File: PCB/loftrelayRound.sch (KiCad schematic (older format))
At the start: 27 parts, among them J1 PowerIn, J2 Load, J3 SenSor, J4 Program, K1 G5Q-14-EU DC5, Q1 2N7002, U1 AP1117-33, U2 PC817, U4 ESP-12E

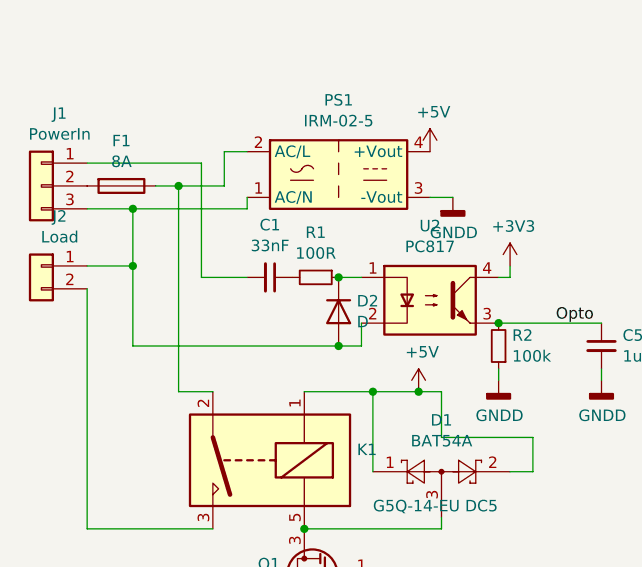
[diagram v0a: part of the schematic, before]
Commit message: Ændret stik
Har ændret til til 3mm mikrofit fjernet C ved optocobler for at undgå stød.
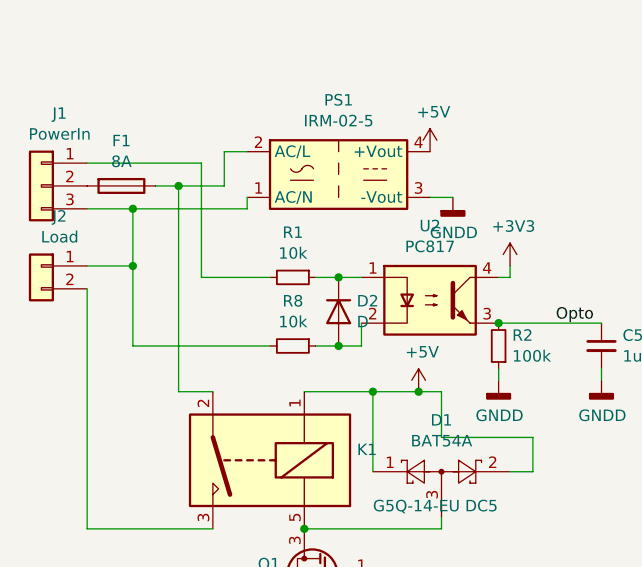
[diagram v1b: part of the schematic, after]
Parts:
- removed C1: 33nF, Capacitors_THT:C_Axial_L5.1mm_D3.1mm_P7.50mm_Horizontal, symbol Device:C_Small
- added R8: 10k, Resistor_SMD:R_1206_3216Metric, symbol Device:R_Small
- J1: footprint Connectors_Molex:Molex_NanoFit_1x03x2.50mm_Straight -> Connector_Molex:Molex_Micro-Fit_3.0_43650-0315_1x03_P3.00mm_Vertical
- J2: footprint Connectors_Molex:Molex_NanoFit_1x02x2.50mm_Straight -> Connector_Molex:Molex_Micro-Fit_3.0_43650-0215_1x02_P3.00mm_Vertical
- R1: value 100R -> 10k; footprint Resistors_SMD:R_1206_HandSoldering -> Resistor_SMD:R_1206_3216Metric
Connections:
- wire segments 85 -> 87
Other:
- moved on the sheet: R1
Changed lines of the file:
@@
-$EndComp
-$Comp
-L Device:C_Small C1
-U 1 1 5BA2C4FB
-P 3350 3050
-F 0 "C1" V 3121 3050 50  0000 C CNN
-F 1 "33nF" V 3212 3050 50  0000 C CNN
-F 2 "Capacitors_THT:C_Axial_L5.1mm_D3.1mm_P7.50mm_Horizontal" H 3350 3050 50  0001 C CNN
-F 3 "~" H 3350 3050 50  0001 C CNN
-	1    3350 3050
-	0    1    1    0
 $EndComp
 $Comp
 L Device:R_Small R1
 U 1 1 5BA2C593
-P 3550 3050
-F 0 "R1" V 3354 3050 50  0000 C CNN
-F 1 "100R" V 3445 3050 50  0000 C CNN
-F 2 "Resistors_SMD:R_1206_HandSoldering" H 3550 3050 50  0001 C CNN
-F 3 "~" H 3550 3050 50  0001 C CNN
-	1    3550 3050
+P 3450 3050
+F 0 "R1" V 3254 3050 50  0000 C CNN
+F 1 "10k" V 3345 3050 50  0000 C CNN
+F 2 "Resistor_SMD:R_1206_3216Metric" H 3450 3050 50  0001 C CNN
+F 3 "~" H 3450 3050 50  0001 C CNN
+	1    3450 3050
 	0    1    1    0
 $EndComp
@@
 F 0 "J1" H 2270 2967 50  0000 C CNN
 F 1 "PowerIn" H 2270 2876 50  0000 C CNN
-F 2 "Connectors_Molex:Molex_NanoFit_1x03x2.50mm_Straight" H 2350 2650 50  0001 C CNN
+F 2 "Connector_Molex:Molex_Micro-Fit_3.0_43650-0315_1x03_P3.00mm_Vertical" H 2350 2650 50  0001 C CNN
 F 3 "~" H 2350 2650 50  0001 C CNN
 	1    2350 2650
@@
 F 0 "J2" H 2270 3217 50  0000 C CNN
 F 1 "Load" H 2270 3126 50  0000 C CNN
-F 2 "Connectors_Molex:Molex_NanoFit_1x02x2.50mm_Straight" H 2350 3000 50  0001 C CNN
+F 2 "Connector_Molex:Molex_Micro-Fit_3.0_43650-0215_1x02_P3.00mm_Vertical" H 2350 3000 50  0001 C CNN
 F 3 "~" H 2350 3000 50  0001 C CNN
 	1    2350 3000
@@
 Wire Wire Line
 	3050 2550 3050 3050
-Wire Wire Line
-	3050 3050 3250 3050
 Connection ~ 2750 2750
 Wire Wire Line
@@
 Wire Wire Line
 	2750 2750 2750 3000
-Wire Wire Line
-	2750 3350 3650 3350
 Connection ~ 3650 3050
-Connection ~ 3650 3350
 Wire Wire Line
 	3650 3350 3750 3350
@@
 Wire Wire Line
 	4350 3250 4800 3250
+$Comp
+L Device:R_Small R8
+U 1 1 5F223F8A
+P 3450 3350
+F 0 "R8" V 3254 3350 50  0000 C CNN
+F 1 "10k" V 3345 3350 50  0000 C CNN
+F 2 "Resistor_SMD:R_1206_3216Metric" H 3450 3350 50  0001 C CNN
+F 3 "~" H 3450 3350 50  0001 C CNN
+	1    3450 3350
+	0    1    1    0
+$EndComp
+Wire Wire Line
+	3650 3050 3550 3050
+Wire Wire Line
+	3050 3050 3350 3050
+Wire Wire Line
+	3650 3350 3550 3350
+Connection ~ 3650 3350
+Wire Wire Line
+	3350 3350 2750 3350
 $EndSCHEMATC

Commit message: Update af komponeter samt ny programmer
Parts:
- Q1: value 2N7002 -> Sq2318AES
- R1: value 10k -> 33K
- R8: value 10k -> 33k
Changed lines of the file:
@@
 P 3450 3050
 F 0 "R1" V 3254 3050 50  0000 C CNN
-F 1 "10k" V 3345 3050 50  0000 C CNN
+F 1 "33K" V 3345 3050 50  0000 C CNN
 F 2 "Resistor_SMD:R_1206_3216Metric" H 3450 3050 50  0001 C CNN
 F 3 "~" H 3450 3050 50  0001 C CNN
@@
 P 3600 4350
 F 0 "Q1" H 3806 4396 50  0000 L CNN
-F 1 "2N7002" H 3806 4305 50  0000 L CNN
+F 1 "Sq2318AES" H 3806 4305 50  0000 L CNN
 F 2 "TO_SOT_Packages_SMD:SOT-23" H 3800 4275 50  0001 L CIN
 F 3 "https://www.fairchildsemi.com/datasheets/2N/2N7002.pdf" H 3600 4350 50  0001 L CNN
@@
 P 3450 3350
 F 0 "R8" V 3254 3350 50  0000 C CNN
-F 1 "10k" V 3345 3350 50  0000 C CNN
+F 1 "33k" V 3345 3350 50  0000 C CNN
 F 2 "Resistor_SMD:R_1206_3216Metric" H 3450 3350 50  0001 C CNN
 F 3 "~" H 3450 3350 50  0001 C CNN

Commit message: 3d footprint
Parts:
- K1: footprint Relays_THT:Relay_SPST_OMRON-G5Q -> Relay_THT:Relay_SPST_Omron-G5Q-1A
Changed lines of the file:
@@
 F 0 "K1" H 2870 3804 50  0000 R CNN
 F 1 "G5Q-14-EU DC5" H 2800 4050 50  0000 R CNN
-F 2 "Relays_THT:Relay_SPST_OMRON-G5Q" H 3650 3800 50  0001 L CNN
+F 2 "Relay_THT:Relay_SPST_Omron-G5Q-1A" H 3650 3800 50  0001 L CNN
 F 3 "https://www.omron.com/ecb/products/pdf/en-g5q.pdf" H 4400 3550 50  0001 C CNN
 	1    3300 3850

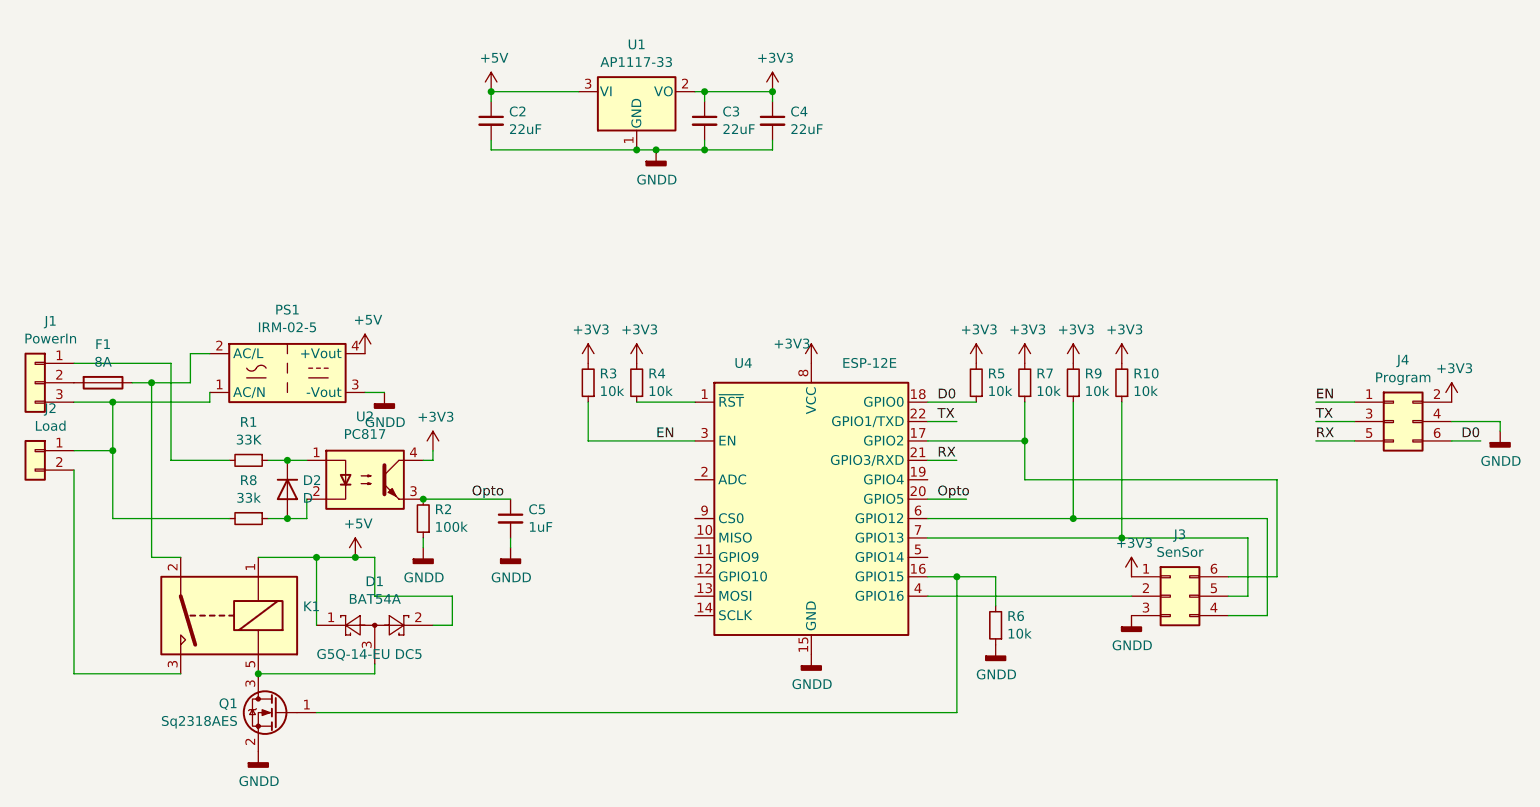
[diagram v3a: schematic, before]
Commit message: Final edit
Ændret LDO , da jeg ikke kunne skaffe den anden på mouser kun i kina, hvilket jeg ikke har tid til. Rettet en bane der kom lidt for tæt og fejlede i første forsøg
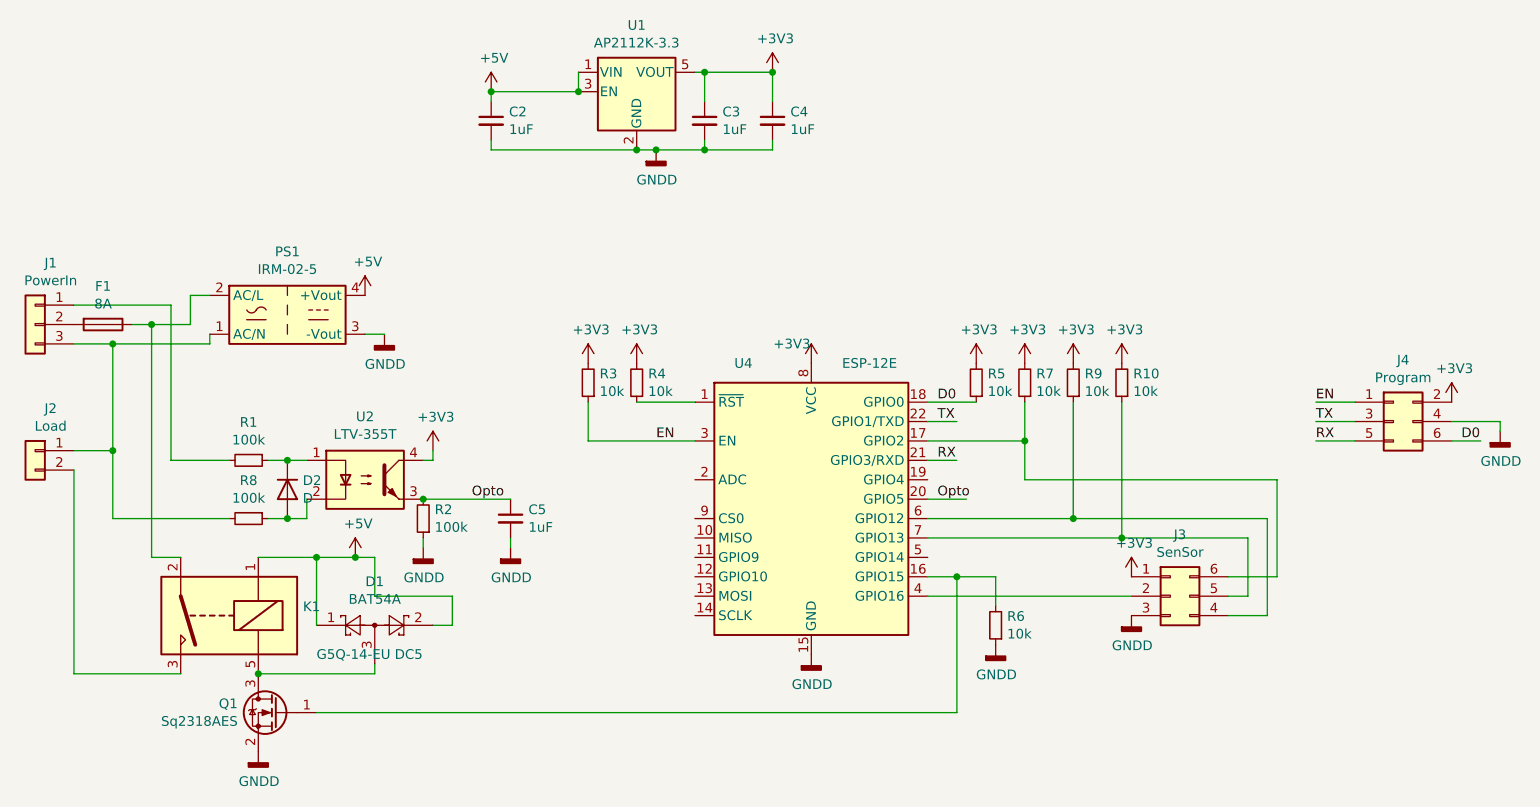
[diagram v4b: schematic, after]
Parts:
- removed U1: AP1117-33, Package_TO_SOT_SMD:SOT-223-3_TabPin2, symbol Regulator_Linear:AP1117-33
- added U1: AP2112K-3.3, Package_TO_SOT_SMD:SOT-23-5, symbol Regulator_Linear:AP2112K-3.3
- C2, C3, C4: value 22uF -> 1uF
- R1: value 33K -> 100k
- R8: value 33k -> 100k
- U2: value PC817 -> LTV-355T
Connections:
- wire segments 87 -> 88
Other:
- moved on the sheet: F1, J1, PS1
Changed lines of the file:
@@
 P 4050 3150
 F 0 "U2" H 4050 3475 50  0000 C CNN
-F 1 "PC817" H 4050 3384 50  0000 C CNN
+F 1 "LTV-355T" H 4050 3384 50  0000 C CNN
 F 2 "Housings_SOIC:SO-4_4.4x3.6mm_Pitch2.54mm" H 3850 2950 50  0001 L CIN
-F 3 "http://www.soselectronic.cz/a_info/resource/d/pc817.pdf" H 4050 3150 50  0001 L CNN
+F 3 "https://www.mouser.dk/datasheet/2/239/LTV-355T%20Series-1308-1175436.pdf" H 4050 3150 50  0001 L CNN
 	1    4050 3150
 	1    0    0    -1
@@
 P 3450 3050
 F 0 "R1" V 3254 3050 50  0000 C CNN
-F 1 "33K" V 3345 3050 50  0000 C CNN
+F 1 "100k" V 3345 3050 50  0000 C CNN
 F 2 "Resistor_SMD:R_1206_3216Metric" H 3450 3050 50  0001 C CNN
 F 3 "~" H 3450 3050 50  0001 C CNN
@@
 L Connector_Generic:Conn_01x03 J1
 U 1 1 5BA2C63B
-P 2350 2650
-F 0 "J1" H 2270 2967 50  0000 C CNN
-F 1 "PowerIn" H 2270 2876 50  0000 C CNN
-F 2 "Connector_Molex:Molex_Micro-Fit_3.0_43650-0315_1x03_P3.00mm_Vertical" H 2350 2650 50  0001 C CNN
-F 3 "~" H 2350 2650 50  0001 C CNN
-	1    2350 2650
+P 2350 2350
+F 0 "J1" H 2270 2667 50  0000 C CNN
+F 1 "PowerIn" H 2270 2576 50  0000 C CNN
+F 2 "Connector_Molex:Molex_Micro-Fit_3.0_43650-0315_1x03_P3.00mm_Vertical" H 2350 2350 50  0001 C CNN
+F 3 "~" H 2350 2350 50  0001 C CNN
+	1    2350 2350
 	-1   0    0    -1
 $EndComp
@@
 L power:GNDD #PWR0113
 U 1 1 5BA2FD4E
-P 4150 2700
-F 0 "#PWR0113" H 4150 2450 50  0001 C CNN
-F 1 "GNDD" H 4154 2545 50  0000 C CNN
-F 2 "" H 4150 2700 50  0001 C CNN
-F 3 "" H 4150 2700 50  0001 C CNN
-	1    4150 2700
+P 4150 2400
+F 0 "#PWR0113" H 4150 2150 50  0001 C CNN
+F 1 "GNDD" H 4154 2245 50  0000 C CNN
+F 2 "" H 4150 2400 50  0001 C CNN
+F 3 "" H 4150 2400 50  0001 C CNN
+	1    4150 2400
 	1    0    0    -1
 $EndComp
@@
 L power:+3V3 #PWR0119
 U 1 1 5BA32682
-P 6150 1150
-F 0 "#PWR0119" H 6150 1000 50  0001 C CNN
-F 1 "+3V3" H 6165 1323 50  0000 C CNN
-F 2 "" H 6150 1150 50  0001 C CNN
-F 3 "" H 6150 1150 50  0001 C CNN
-	1    6150 1150
+P 6150 1050
+F 0 "#PWR0119" H 6150 900 50  0001 C CNN
+F 1 "+3V3" H 6165 1223 50  0000 C CNN
+F 2 "" H 6150 1050 50  0001 C CNN
+F 3 "" H 6150 1050 50  0001 C CNN
+	1    6150 1050
 	1    0    0    -1
 $EndComp
@@
 P 4700 1300
 F 0 "C2" H 4792 1346 50  0000 L CNN
-F 1 "22uF" H 4792 1255 50  0000 L CNN
+F 1 "1uF" H 4792 1255 50  0000 L CNN
 F 2 "Capacitors_SMD:C_0805_HandSoldering" H 4700 1300 50  0001 C CNN
 F 3 "~" H 4700 1300 50  0001 C CNN
@@
 P 5800 1300
 F 0 "C3" H 5892 1346 50  0000 L CNN
-F 1 "22uF" H 5892 1255 50  0000 L CNN
+F 1 "1uF" H 5892 1255 50  0000 L CNN
 F 2 "Capacitors_SMD:C_0805_HandSoldering" H 5800 1300 50  0001 C CNN
 F 3 "~" H 5800 1300 50  0001 C CNN
@@
 P 6150 1300
 F 0 "C4" H 6242 1346 50  0000 L CNN
-F 1 "22uF" H 6242 1255 50  0000 L CNN
+F 1 "1uF" H 6242 1255 50  0000 L CNN
 F 2 "Capacitors_SMD:C_0805_HandSoldering" H 6150 1300 50  0001 C CNN
 F 3 "~" H 6150 1300 50  0001 C CNN
@@
 	1    0    0    -1
 $EndComp
-Wire Wire Line
-	6150 1200 6150 1150
-Wire Wire Line
-	6150 1150 5800 1150
-Connection ~ 6150 1150
-Wire Wire Line
-	5800 1200 5800 1150
-Connection ~ 5800 1150
-Wire Wire Line
-	5800 1150 5750 1150
 Wire Wire Line
 	4700 1400 4700 1450
@@
 	5550 1450 5800 1450
 Wire Wire Line
-	3250 2700 3250 2750
-Wire Wire Line
-	2550 2550 3050 2550
-Wire Wire Line
-	3050 2550 3050 3050
-Connection ~ 2750 2750
-Wire Wire Line
-	2750 2750 2550 2750
+	3250 2400 3250 2450
+Wire Wire Line
+	2550 2250 3050 2250
+Connection ~ 2750 2450
+Wire Wire Line
+	2750 2450 2550 2450
 $Comp
 L Device:D D2
@@
 Wire Wire Line
 	3750 3250 3750 3350
-Wire Wire Line
-	2750 2750 2750 3000
 Connection ~ 3650 3050
 Wire Wire Line
@@
 $EndComp
 Wire Wire Line
-	4700 1450 5450 1450
-$Comp
-L Regulator_Linear:AP1117-33 U1
-U 1 1 5E339999
-P 5450 1150
-F 0 "U1" H 5450 1392 50  0000 C CNN
-F 1 "AP1117-33" H 5450 1301 50  0000 C CNN
-F 2 "Package_TO_SOT_SMD:SOT-223-3_TabPin2" H 5450 1350 50  0001 C CNN
-F 3 "http://www.diodes.com/datasheets/AP1117.pdf" H 5550 900 50  0001 C CNN
-	1    5450 1150
-	1    0    0    -1
-$EndComp
-Connection ~ 5450 1450
-Wire Wire Line
-	5450 1450 5550 1450
-Wire Wire Line
 	4700 1150 5150 1150
 $Comp
 L loftrelayRound-rescue:IRM-02-5-Converter_ACDC PS1
 U 1 1 5E33B388
-P 3650 2600
-F 0 "PS1" H 3650 2925 50  0000 C CNN
-F 1 "IRM-02-5" H 3650 2834 50  0000 C CNN
-F 2 "Converter_ACDC:Converter_ACDC_MeanWell_IRM-02-xx_THT" H 3650 2300 50  0001 C CNN
-F 3 "http://www.meanwell.com/productPdf.aspx?i=675" H 4050 2250 50  0001 C CNN
-	1    3650 2600
-	1    0    0    -1
-$EndComp
-Wire Wire Line
-	3150 2500 3250 2500
-Wire Wire Line
-	3150 2500 3150 2650
-Wire Wire Line
-	4150 2700 4050 2700
+P 3650 2300
+F 0 "PS1" H 3650 2625 50  0000 C CNN
+F 1 "IRM-02-5" H 3650 2534 50  0000 C CNN
+F 2 "Converter_ACDC:Converter_ACDC_MeanWell_IRM-02-xx_THT" H 3650 2000 50  0001 C CNN
+F 3 "http://www.meanwell.com/productPdf.aspx?i=675" H 4050 1950 50  0001 C CNN
+	1    3650 2300
+	1    0    0    -1
+$EndComp
+Wire Wire Line
+	3150 2200 3250 2200
+Wire Wire Line
+	3150 2200 3150 2350
+Wire Wire Line
+	4150 2400 4050 2400
 $Comp
 L power:+5V #PWR0122
 U 1 1 5E33E28D
-P 4050 2500
-F 0 "#PWR0122" H 4050 2350 50  0001 C CNN
-F 1 "+5V" H 4065 2673 50  0000 C CNN
-F 2 "" H 4050 2500 50  0001 C CNN
-F 3 "" H 4050 2500 50  0001 C CNN
-	1    4050 2500
+P 4050 2200
+F 0 "#PWR0122" H 4050 2050 50  0001 C CNN
+F 1 "+5V" H 4065 2373 50  0000 C CNN
+F 2 "" H 4050 2200 50  0001 C CNN
+F 3 "" H 4050 2200 50  0001 C CNN
+	1    4050 2200
 	1    0    0    -1
 $EndComp
@@
 Wire Wire Line
 	2550 3000 2750 3000
-Connection ~ 2750 3000
 Wire Wire Line
 	2750 3000 2750 3350
 Wire Wire Line
-	2750 2750 3250 2750
+	2750 2450 3250 2450
 $Comp
 L Device:Fuse F1
 U 1 1 5E369492
-P 2700 2650
-F 0 "F1" V 2503 2650 50  0000 C CNN
-F 1 "8A" V 2594 2650 50  0000 C CNN
-F 2 "SMD_Packages:Fuse_SMD" V 2630 2650 50  0001 C CNN
-F 3 "~" H 2700 2650 50  0001 C CNN
-	1    2700 2650
+P 2700 2350
+F 0 "F1" V 2503 2350 50  0000 C CNN
+F 1 "8A" V 2594 2350 50  0000 C CNN
+F 2 "SMD_Packages:Fuse_SMD" V 2630 2350 50  0001 C CNN
+F 3 "~" H 2700 2350 50  0001 C CNN
+	1    2700 2350
 	0    1    1    0
 $EndComp
 Wire Wire Line
-	2850 2650 2950 2650
-Wire Wire Line
-	2950 2650 2950 3550
+	2850 2350 2950 2350
 Wire Wire Line
 	2950 3550 3100 3550
-Connection ~ 2950 2650
-Wire Wire Line
-	2950 2650 3150 2650
+Connection ~ 2950 2350
+Wire Wire Line
+	2950 2350 3150 2350
 Wire Wire Line
 	7450 2950 7450 3150
@@
 P 3450 3350
 F 0 "R8" V 3254 3350 50  0000 C CNN
-F 1 "33k" V 3345 3350 50  0000 C CNN
+F 1 "100k" V 3345 3350 50  0000 C CNN
 F 2 "Resistor_SMD:R_1206_3216Metric" H 3450 3350 50  0001 C CNN
 F 3 "~" H 3450 3350 50  0001 C CNN
@@
 Wire Wire Line
 	3350 3350 2750 3350
+Wire Wire Line
+	3050 2250 3050 3050
+Wire Wire Line
+	2950 2350 2950 3550
+Wire Wire Line
+	2750 2450 2750 3000
+Connection ~ 2750 3000
+$Comp
+L Regulator_Linear:AP2112K-3.3 U1
+U 1 1 5F508A31
+P 5450 1150
+F 0 "U1" H 5450 1492 50  0000 C CNN
+F 1 "AP2112K-3.3" H 5450 1401 50  0000 C CNN
+F 2 "Package_TO_SOT_SMD:SOT-23-5" H 5450 1475 50  0001 C CNN
+F 3 "https://www.diodes.com/assets/Datasheets/AP2112.pdf" H 5450 1250 50  0001 C CNN
+	1    5450 1150
+	1    0    0    -1
+$EndComp
+Wire Wire Line
+	4700 1450 5450 1450
+Connection ~ 5450 1450
+Wire Wire Line
+	5450 1450 5550 1450
+Wire Wire Line
+	6150 1050 6150 1200
+Wire Wire Line
+	6150 1050 5800 1050
+Connection ~ 6150 1050
+Connection ~ 5800 1050
+Wire Wire Line
+	5800 1050 5750 1050
+Wire Wire Line
+	5150 1150 5150 1050
+Connection ~ 5150 1150
+Wire Wire Line
+	5800 1050 5800 1200
 $EndSCHEMATC
